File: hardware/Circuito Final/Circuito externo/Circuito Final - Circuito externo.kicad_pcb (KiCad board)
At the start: 2 copper layers, 9 parts, among them J1 Conn_02x19_Odd_Even, J2 Conn_02x19_Odd_Even, J3 Conn_01x02, J4 Conn_01x02

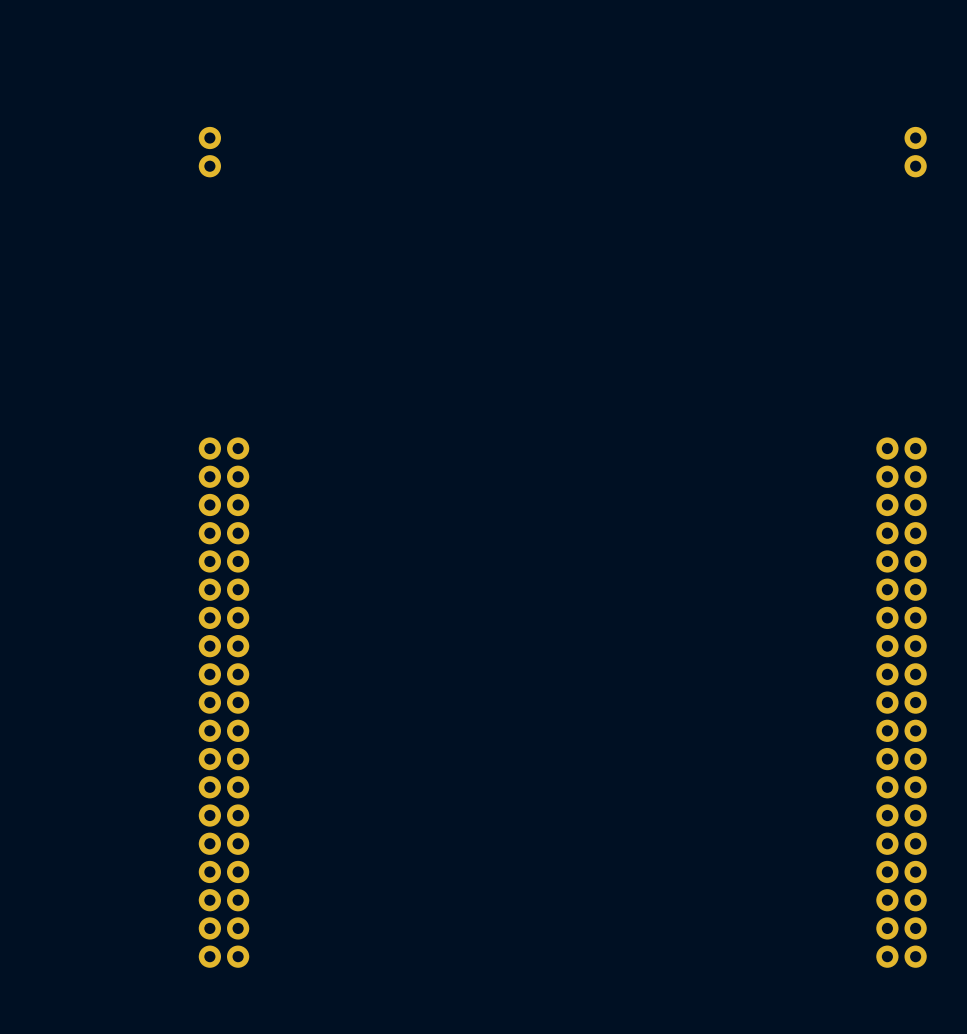
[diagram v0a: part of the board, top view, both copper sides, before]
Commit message: subida del modelo 3D del controlador y update del kicad correspondiente
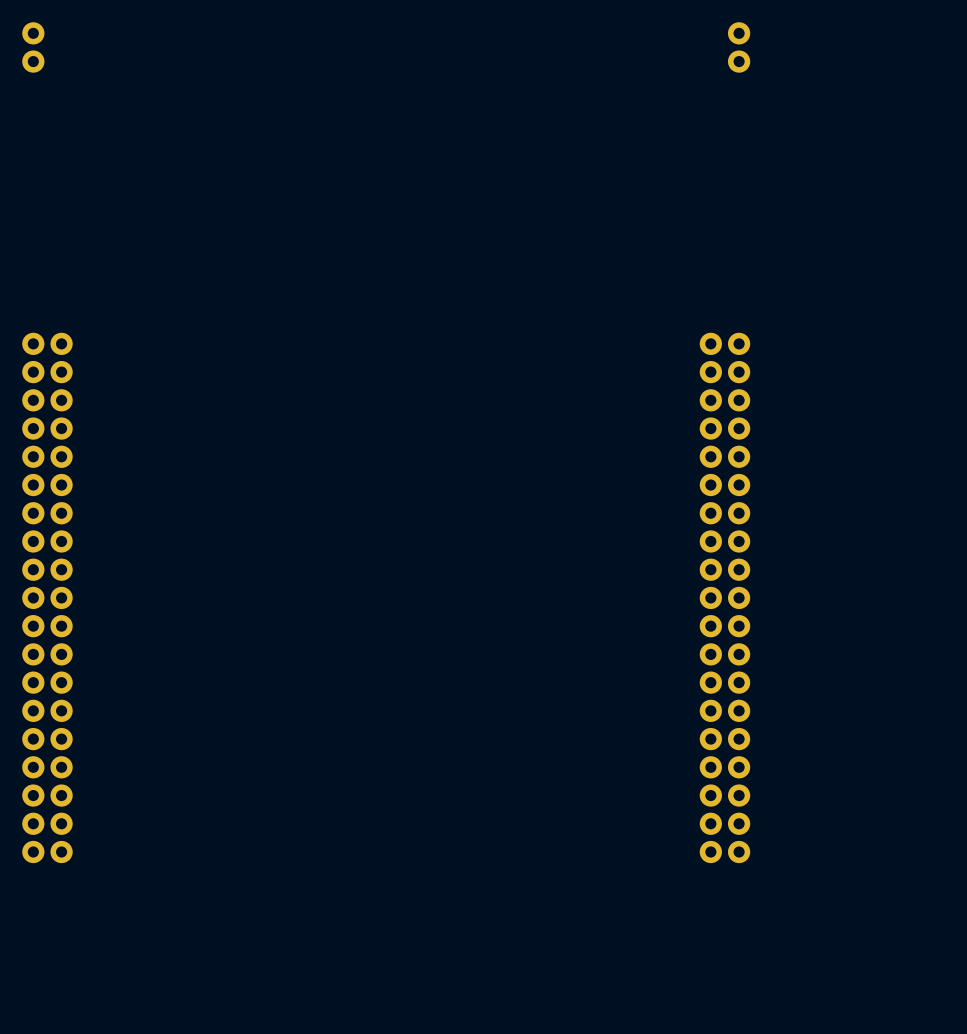
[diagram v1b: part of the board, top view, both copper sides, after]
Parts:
- added STM32: STM32, Library - STM32:STM32, B.Cu at (112.1, 80.0)
- moved J1 18.5 mm to (141.3, 70.8)
- moved J2 18.5 mm to (80.3, 70.8)
- moved J3 18.5 mm to (143.8, 42.9)
- moved J4 18.5 mm to (80.3, 42.9)
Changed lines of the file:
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@@
 	(footprint "Connector_PinSocket_2.54mm:PinSocket_1x02_P2.54mm_Vertical"
 		(layer "B.Cu")
-		(at 96.204589 52.287157 180)
+		(at 80.32 42.87 180)
 		(descr "Through hole straight socket strip, 1x02, 2.54mm pitch, single row (from Kicad 4.0.7), script generated")
 		(tags "Through hole socket strip THT 1x02 2.54mm single row")
@@
 		)
 	)
+	(footprint "Library - STM32:STM32"
+		(layer "B.Cu")
+		(at 112.13 80 180)
+		(property "Reference" "STM32"
+			(at 0 0.5 0)
+			(unlocked yes)
+			(layer "B.SilkS")
+			(effects
+				(font
+					(size 1 1)
+					(thickness 0.1)
+				)
+				(justify mirror)
+			)
+		)
+		(property "Value" "STM32"
+			(at 0 -1 0)
+			(unlocked yes)
+			(layer "B.Fab")
+			(effects
+				(font
+					(size 1 1)
+					(thickness 0.15)
+				)
+				(justify mirror)
+			)
+		)
+		(property "Datasheet" ""
+			(at 0 0 0)
+			(unlocked yes)
+			(layer "B.Fab")
+			(hide yes)
+			(effects
+				(font
+					(size 1 1)
+					(thickness 0.15)
+				)
+				(justify mirror)
+			)
+		)
+		(property "Description" ""
+			(at 0 0 0)
+			(unlocked yes)
+			(layer "B.Fab")
+			(hide yes)
+			(effects
+				(font
+					(size 1 1)
+					(thickness 0.15)
+				)
+				(justify mirror)
+			)
+		)
+		(attr smd)
+		(duplicate_pad_numbers_are_jumpers no)
+		(fp_rect
+			(start -35 41.250479)
+			(end 35 -41.249521)
+			(stroke
+				(width 0.1)
+				(type default)
+			)
+			(fill no)
+			(layer "B.SilkS")
+		)
+		(fp_text user "STM32 Nucleo 64 bits"
+			(at 0 -2.5 0)
+			(unlocked yes)
+			(layer "B.Fab")
+			(effects
+				(font
+					(size 1 1)
+					(thickness 0.15)
+				)
+				(justify mirror)
+			)
+		)
+		(embedded_fonts no)
+		(model "C:/Users/Sebas/Desktop/Trabajo Profesional de Ingeniería Electrónica/Tesis/hardware/PCB/Modelos 3D/NUCLEO-60-F401.STEP"
+			(offset
+				(xyz 9 -39 11)
+			)
+			(scale
+				(xyz 1 1 1)
+			)
+			(rotate
+				(xyz -0 -0 -0)
+			)
+		)
+	)
 	(footprint "Connector_PinSocket_2.54mm:PinSocket_1x02_P2.54mm_Vertical"
 		(layer "B.Cu")
-		(at 159.704589 52.287157 180)
+		(at 143.82 42.87 180)
 		(descr "Through hole straight socket strip, 1x02, 2.54mm pitch, single row (from Kicad 4.0.7), script generated")
 		(tags "Through hole socket strip THT 1x02 2.54mm single row")
@@
 	(footprint "Connector_PinSocket_2.54mm:PinSocket_2x19_P2.54mm_Vertical"
 		(layer "B.Cu")
-		(at 96.204589 80.227157 180)
+		(at 80.32 70.81 180)
 		(descr "Through hole straight socket strip, 2x19, 2.54mm pitch, double rows (from Kicad 4.0.7), script generated")
 		(tags "Through hole socket strip THT 2x19 2.54mm double row")
@@
 	(footprint "Connector_PinSocket_2.54mm:PinSocket_2x19_P2.54mm_Vertical"
 		(layer "B.Cu")
-		(at 157.164589 80.227157 180)
+		(at 141.28 70.81 180)
 		(descr "Through hole straight socket strip, 2x19, 2.54mm pitch, double rows (from Kicad 4.0.7), script generated")
 		(tags "Through hole socket strip THT 2x19 2.54mm double row")
@@
 	)
 	(group ""
-		(members "077800ea-51d3-444d-a0ff-763eaa416d09" "2a27c529-014b-41d7-8266-267dde69ec85"
-			"6f2024a2-93af-43c2-8a9b-4e9cedf6118a" "916219ae-c4ef-4e1c-82f3-9a28930fea9d"
+		(members "077800ea-51d3-444d-a0ff-763eaa416d09" "286afc46-4049-4cbd-a74d-341db855bc9f"
+			"2a27c529-014b-41d7-8266-267dde69ec85" "6f2024a2-93af-43c2-8a9b-4e9cedf6118a"
+			"916219ae-c4ef-4e1c-82f3-9a28930fea9d"
 		)
 	)

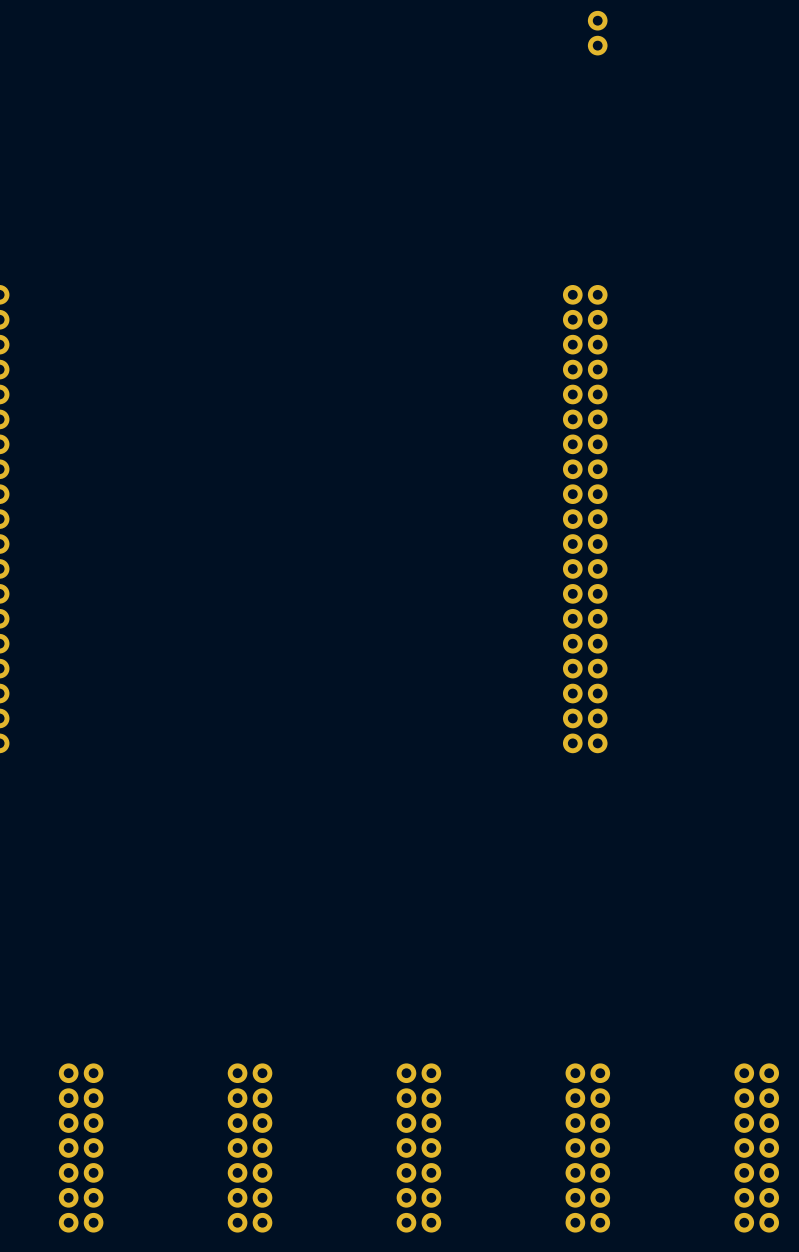
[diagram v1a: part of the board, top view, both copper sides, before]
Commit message: Subida del circuito con el dibujo de la pilita en el cobre
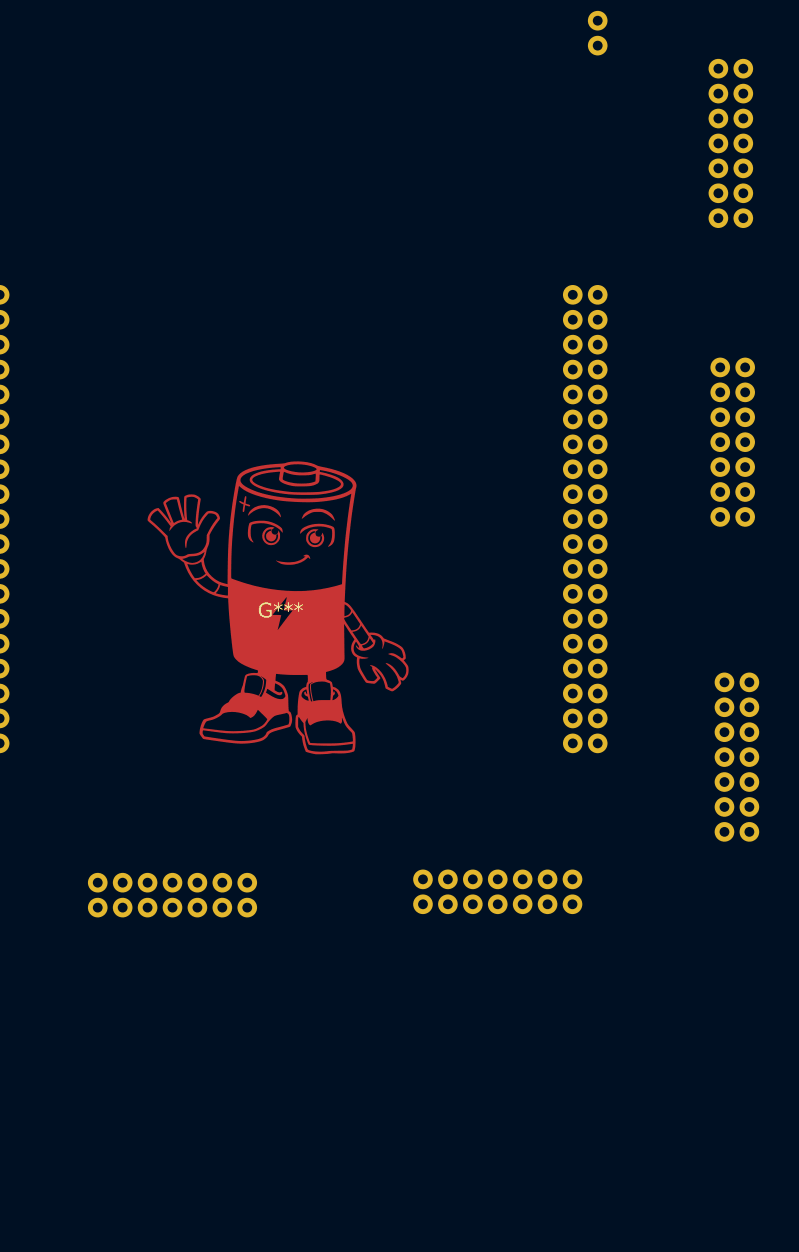
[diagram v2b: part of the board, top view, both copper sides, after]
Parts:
- added G***: LOGO, Pilita:pilita, F.Cu at (111.5, 103.0)
- moved Jsalida_1 87.3 mm to (156.1, 63.0), turned to 0 degrees
- moved Jsalida_2 58.0 mm to (156.3, 93.5), turned to 0 degrees
- moved Jsalida_3 38.7 mm to (156.7, 125.5), turned to 0 degrees
- moved Jsalida_4 25.7 mm to (126.0, 130.4), turned to -90 degrees
- moved Jsalida_5 19.4 mm to (92.9, 130.7), turned to -90 degrees

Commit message: update pcb externo
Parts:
- removed Jsalida_5: Conn_02x07_Odd_Even, Connector_IDC:IDC-Header_2x07_P2.54mm_Horizontal
- added Bornera1: Conn_01x02_Socket, Huellas:TerminalBlock_bornier-2_P5.08mm, B.Cu at (120.9, 130.5)
- added C1: 10u, Capacitor_SMD:C_1206_3216Metric_Pad1.33x1.80mm_HandSolder, F.Cu at (109.9, 128.0)
- added J5: Conn_02x04_Counter_Clockwise, Connector_PinHeader_2.54mm:PinHeader_2x04_P2.54mm_Vertical, B.Cu at (99.0, 129.5)
- moved Jsalida_4 100.7 mm to (68.5, 47.8), turned to 180 degrees
- moved Jsalida_3 99.7 mm to (68.0, 80.0), turned to 180 degrees
- moved Jsalida_2 1.79 mm to (156.3, 95.2)
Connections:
- J1 pad 1: unconnected-(J1-Pin_1-Pad1) -> /clk_latch
- J1 pad 2: unconnected-(J1-Pin_2-Pad2) -> /clk_shift
- J1 pad 20: unconnected-(J1-Pin_20-Pad20) -> GND
- J1 pad 24: unconnected-(J1-Pin_24-Pad24) -> /Data_2
- J1 pad 4: unconnected-(J1-Pin_4-Pad4) -> /Data_1
- J2 pad 1: unconnected-(J2-Pin_1-Pad1) -> /Bit_0
- J2 pad 10: unconnected-(J2-Pin_10-Pad10) -> GND
- J2 pad 19: unconnected-(J2-Pin_19-Pad19) -> GND
- J2 pad 2: unconnected-(J2-Pin_2-Pad2) -> /Bit_1
- J2 pad 31: unconnected-(J2-Pin_31-Pad31) -> GND
- J2 pad 4: unconnected-(J2-Pin_4-Pad4) -> /Bit_2

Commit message: version actualizada del pcb externo
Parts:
- removed J5: Conn_02x04_Counter_Clockwise, Connector_PinHeader_2.54mm:PinHeader_2x04_P2.54mm_Vertical
- added SW1: SW_SPDT, Button_Switch_THT:SW_Slide_SPDT_Straight_CK_OS102011MS2Q, F.Cu at (141.0, 128.4)
- added SW2: SW_DIP_x04, Button_Switch_THT:SW_DIP_SPSTx04_Slide_9.78x12.34mm_W7.62mm_P2.54mm, F.Cu at (100.6, 124.8)

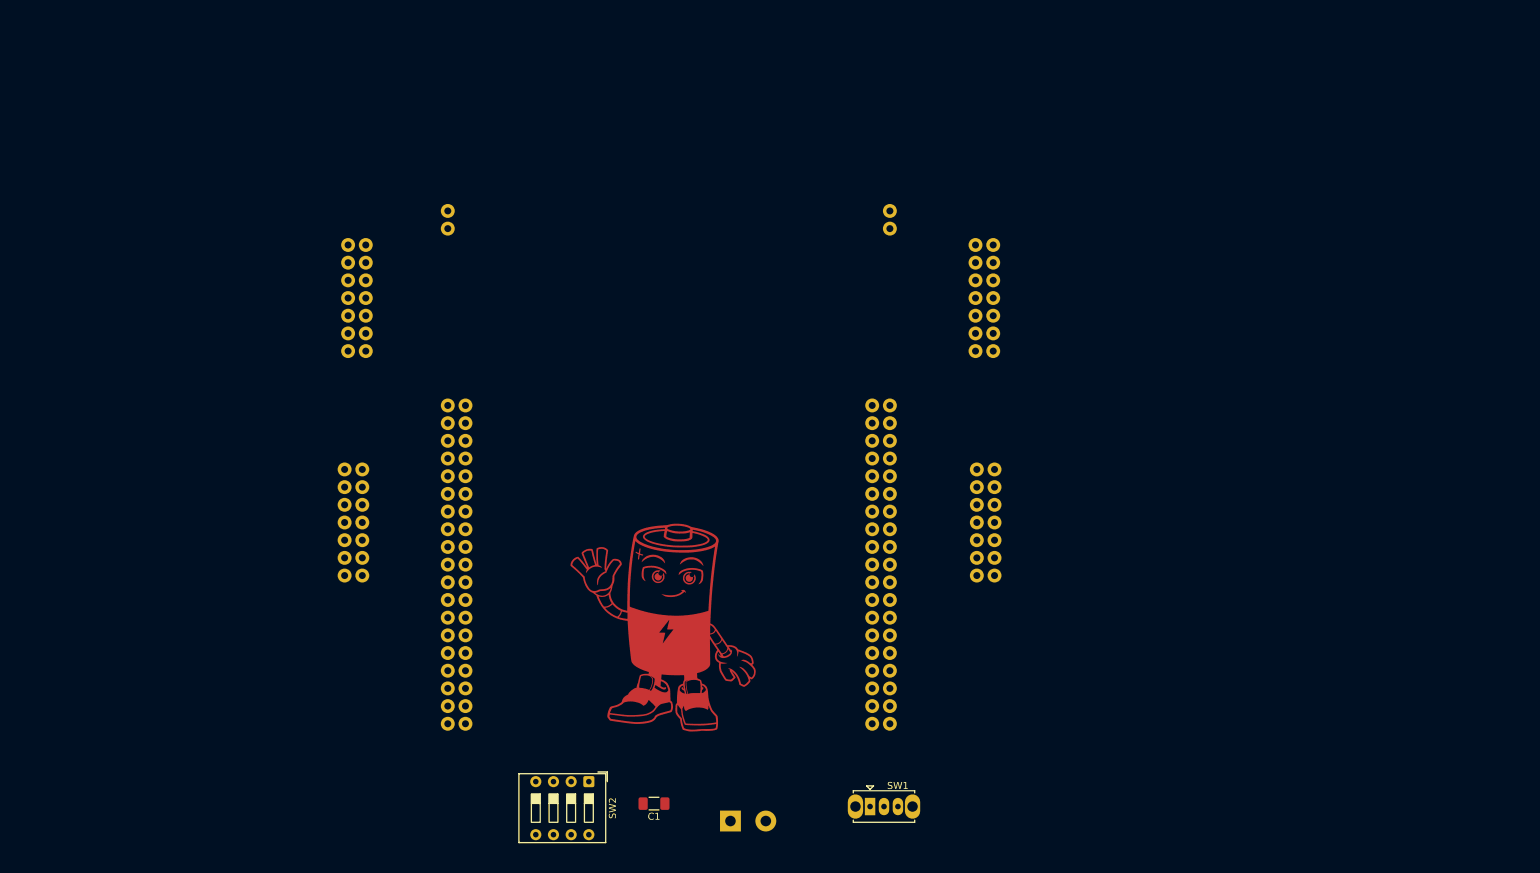
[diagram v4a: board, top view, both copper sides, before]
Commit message: update pcb circuito externo
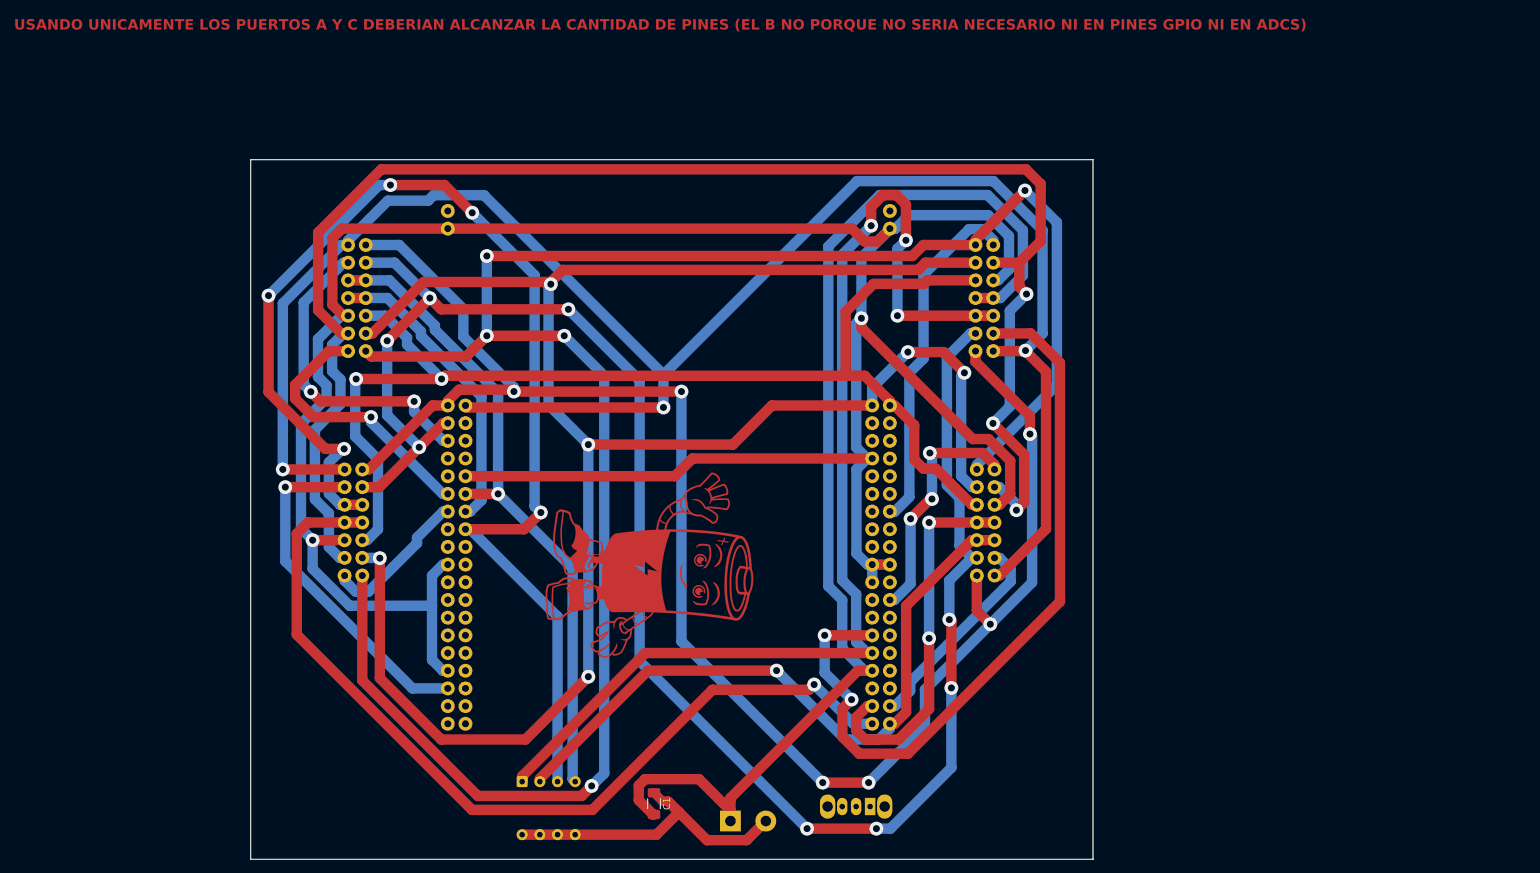
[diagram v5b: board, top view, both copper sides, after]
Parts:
- SW1, SW2: moved to B.Cu
- moved SW2 9.58 mm to (91.0, 124.8)
- moved G*** 9.34 mm to (109.0, 94.0), turned to -90 degrees
- turned C1 to -90 degrees
- turned SW1 to 180 degrees
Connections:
- J1 pad 14: unconnected-(J1-Pin_14-Pad14) -> /Data_1
- J1 pad 27: unconnected-(J1-Pin_27-Pad27) -> /salida_adc_1
- J1 pad 29: unconnected-(J1-Pin_29-Pad29) -> /bus_pos_1
- J1 pad 31: unconnected-(J1-Pin_31-Pad31) -> /bus_neg_1
- J1 pad 35: unconnected-(J1-Pin_35-Pad35) -> /bus_neg_2
- J1 pad 36: unconnected-(J1-Pin_36-Pad36) -> /salida_adc_2
- J1 pad 37: unconnected-(J1-Pin_37-Pad37) -> /bus_neg_3
- J1 pad 38: unconnected-(J1-Pin_38-Pad38) -> /bus_pos_2
- J1 pad 4: /Data_1 -> unconnected-(J1-Pin_4-Pad4)
- J2 pad 1: /Bit_0 -> /Bit_1
- J2 pad 11: unconnected-(J2-Pin_11-Pad11) -> /Data_4
- J2 pad 12: unconnected-(J2-Pin_12-Pad12) -> /bus_pos_4
- J2 pad 13: unconnected-(J2-Pin_13-Pad13) -> /Data_3
- J2 pad 14: unconnected-(J2-Pin_14-Pad14) -> /bus_neg_4
- J2 pad 16: unconnected-(J2-Pin_16-Pad16) -> /bus_pos_3
- J2 pad 2: /Bit_1 -> /Bit_0
- J2 pad 3: unconnected-(J2-Pin_3-Pad3) -> /Bit_2
- J2 pad 33: unconnected-(J2-Pin_33-Pad33) -> /salida_adc_3
- J2 pad 4: /Bit_2 -> unconnected-(J2-Pin_4-Pad4)
- J2 pad 5: unconnected-(J2-Pin_5-Pad5) -> /salida_adc_4
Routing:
- net GND: track 0.00 -> 361.3 mm, vias 0 -> 2
- net /Vcc_out: track 0.00 -> 293.1 mm, vias 0 -> 5
- net /clk_latch: track 0.00 -> 288.3 mm, vias 0 -> 6
- net /Bit_0: track 0.00 -> 267.0 mm, vias 0 -> 3
- net /Bit_2: track 0.00 -> 255.2 mm, vias 0 -> 8
- net /Bit_1: track 0.00 -> 237.8 mm, vias 0 -> 6
- net /reset: track 0.00 -> 224.7 mm, vias 0 -> 3
- net /bus_pos_3: track 0.00 -> 179.6 mm, vias 0 -> 5
- net /clk_shift: track 0.00 -> 171.1 mm, vias 0 -> 2
- net /bus_neg_1: track 0.00 -> 163.7 mm
- net /bus_pos_1: track 0.00 -> 162.9 mm, vias 0 -> 3
- net /bus_neg_3: track 0.00 -> 127.4 mm, vias 0 -> 1
- net /salida_adc_1: track 0.00 -> 110.5 mm, vias 0 -> 2
- net /bus_pos_2: track 0.00 -> 97.5 mm, vias 0 -> 1
- net /bus_pos_4: track 0.00 -> 93.7 mm, vias 0 -> 1
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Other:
- board outline added: 121 x 100.5 mm
- board text added: "USANDO UNICAMENTE LOS PUERTOS A Y C DEBERIAN ALCANZAR LA CANTIDAD DE PINES (EL B NO PORQUE NO SERIA NECESARIO NI EN PINES GPIO NI EN ADCS)"

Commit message: update pcb central
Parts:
- moved G*** 118.5 mm to (220.5, 54.0), turned to 0 degrees
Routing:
- net /Vcc_out: track 293.1 -> 155.1 mm, vias 5 -> 2
- net /Bit_1: track 237.8 -> 153.9 mm, vias 6 -> 4
- net /Bit_2: track 255.2 -> 176.2 mm, vias 8 -> 4
- net /bus_pos_3: track 179.6 -> 106.2 mm, vias 5 -> 2
- net /reset: track 224.7 -> 293.8 mm, vias 3 -> 5
- net GND: track 361.3 -> 410.1 mm, vias 2 -> 7
- net /clk_shift: track 171.1 -> 214.2 mm, vias 2 -> 4
- net /salida_adc_3: track 50.1 -> 90.6 mm, vias 1 -> 2
- net /bus_neg_1: track 163.7 -> 127.5 mm, vias 0 -> 3
- net /bus_pos_1: track 162.9 -> 131.1 mm, vias 3 -> 4
- net /salida_adc_4: track 45.4 -> 73.8 mm
- net /Bit_0: track 267.0 -> 293.2 mm, vias 3 -> 4
- net /Data_3: track 21.4 -> 0.00 mm
- net /clk_latch: track 288.3 -> 301.8 mm, vias 6 -> 5
- net /bus_neg_2: track 53.8 -> 64.9 mm
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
